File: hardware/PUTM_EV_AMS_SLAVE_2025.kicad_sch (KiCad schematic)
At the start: 19 parts, among them J1 M80-5100405, J2 M80-5100405, J4 IDC24

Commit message: routing 80-90% done
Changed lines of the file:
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@@
-		(length 2.54)
-		(shape round)
-		(at 257.81 -50.8 180)
-		(fields_autoplaced yes)
-		(effects
-			(font
-				(size 1.27 1.27)
-			)
-			(justify right bottom)
-		)
-		(property "Netclass" "DP_50Ohm"
-			(at 258.5085 -48.26 0)
-			(effects
-				(font
-					(size 1.27 1.27)
-					(italic yes)
-				)
-				(justify left)
-			)
-		)
-	)
-	(netclass_flag ""
 		(length 2.54)
 		(shape round)
@@
 		(length 2.54)
 		(shape round)
-		(at 278.13 -53.34 0)
-		(fields_autoplaced yes)
+		(at 226.06 99.06 180)
+		(effects
+			(font
+				(size 1.27 1.27)
+			)
+			(justify right bottom)
+		)
+		(property "Netclass" "DP_50Ohm"
+			(at 226.06 102.87 90)
+			(effects
+				(font
+					(size 1.27 1.27)
+					(italic yes)
+				)
+				(justify right)
+			)
+		)
+	)
+	(netclass_flag ""
+		(length 2.54)
+		(shape round)
+		(at 34.29 101.6 180)
+		(effects
+			(font
+				(size 1.27 1.27)
+			)
+			(justify right bottom)
+		)
+		(property "Netclass" "DP_50Ohm"
+			(at 34.29 105.41 90)
+			(effects
+				(font
+					(size 1.27 1.27)
+					(italic yes)
+				)
+				(justify right)
+			)
+		)
+	)
+	(netclass_flag ""
+		(length 2.54)
+		(shape round)
+		(at 261.62 93.98 0)
 		(effects
 			(font
@@
 		)
 		(property "Netclass" "DP_50Ohm"
-			(at 278.8285 -55.88 0)
-			(effects
-				(font
-					(size 1.27 1.27)
-					(italic yes)
-				)
-				(justify left)
-			)
-		)
-	)
-	(netclass_flag ""
-		(length 2.54)
-		(shape round)
-		(at 226.06 99.06 180)
-		(effects
-			(font
-				(size 1.27 1.27)
-			)
-			(justify right bottom)
-		)
-		(property "Netclass" "DP_50Ohm"
-			(at 226.06 102.87 90)
-			(effects
-				(font
-					(size 1.27 1.27)
-					(italic yes)
-				)
-				(justify right)
-			)
-		)
-	)
-	(netclass_flag ""
-		(length 2.54)
-		(shape round)
-		(at 34.29 101.6 180)
-		(effects
-			(font
-				(size 1.27 1.27)
-			)
-			(justify right bottom)
-		)
-		(property "Netclass" "DP_50Ohm"
-			(at 34.29 105.41 90)
-			(effects
-				(font
-					(size 1.27 1.27)
-					(italic yes)
-				)
-				(justify right)
-			)
-		)
-	)
-	(netclass_flag ""
-		(length 2.54)
-		(shape round)
-		(at 261.62 93.98 0)
-		(effects
-			(font
-				(size 1.27 1.27)
-			)
-			(justify left bottom)
-		)
-		(property "Netclass" "DP_50Ohm"
 			(at 261.62 80.01 90)
 			(effects
@@
 				)
 				(justify right)
-			)
-		)
-	)
-	(netclass_flag ""
-		(length 2.54)
-		(shape round)
-		(at 278.13 -50.8 180)
-		(fields_autoplaced yes)
-		(effects
-			(font
-				(size 1.27 1.27)
-			)
-			(justify right bottom)
-		)
-		(property "Netclass" "DP_50Ohm"
-			(at 278.8285 -48.26 0)
-			(effects
-				(font
-					(size 1.27 1.27)
-					(italic yes)
-				)
-				(justify left)
 			)
 		)
@@
 				)
 				(justify right)
-			)
-		)
-	)
-	(netclass_flag ""
-		(length 2.54)
-		(shape round)
-		(at 257.81 -53.34 0)
-		(fields_autoplaced yes)
-		(effects
-			(font
-				(size 1.27 1.27)
-			)
-			(justify left bottom)
-		)
-		(property "Netclass" "DP_50Ohm"
-			(at 258.5085 -55.88 0)
-			(effects
-				(font
-					(size 1.27 1.27)
-					(italic yes)
-				)
-				(justify left)
 			)
 		)
@@
 		(dnp no)
 		(property "Reference" "R55"
-			(at 189.23 91.2114 90)
+			(at 189.23 88.9 90)
 			(effects
 				(font
@@
 		)
 		(property "Value" "1k"
-			(at 189.23 88.9 90)
-			(effects
-				(font
+			(at 189.23 91.44 90)
+			(effects
+				(font

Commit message: bom update
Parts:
- C46, C47, C48, C49: Mouser Part Number (none) -> 581-06033A221JAT2A
- J4: Mouser Part Number (none) -> 737-BHR-24-VSG-SMT
- L1, L2: Mouser Part Number (none) -> 673-PE-1812AGC101STS
- R55, R58: Mouser Part Number 603-RT0603FRE07330RL -> --
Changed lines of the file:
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@@
+			)
+		)
+		(property "Arrow Part Number" ""
+			(at 144.78 41.91 0)
+			(effects
+				(font
+					(size 1.27 1.27)
+				)
+				(hide yes)
+			)
+		)
+		(property "Arrow Price/Stock" ""
+			(at 144.78 41.91 0)
+			(effects
+				(font
+					(size 1.27 1.27)
+				)
+				(hide yes)
+			)
+		)
+		(property "Mouser Part Number" "737-BHR-24-VSG-SMT"
+			(at 144.78 41.91 0)
+			(effects
+				(font
+					(size 1.27 1.27)
+				)
+				(hide yes)
 			)
 		)
@@
 			)
 		)
-		(property "Mouser Part Number" "603-RT0603FRE07330RL"
+		(property "Mouser Part Number" "--"
 			(at 189.23 93.98 0)
 			(effects
@@
 		)
 		(property "TME Electronic Components Price/Stock" ""
+			(at 25.4 91.44 0)
+			(effects
+				(font
+					(size 1.27 1.27)
+				)
+				(hide yes)
+			)
+		)
+		(property "Arrow Part Number" ""
+			(at 25.4 91.44 0)
+			(effects
+				(font
+					(size 1.27 1.27)
+				)
+				(hide yes)
+			)
+		)
+		(property "Arrow Price/Stock" ""
 			(at 25.4 91.44 0)
 			(effects
@@
 			)
 		)
+		(property "Arrow Part Number" ""
+			(at 238.76 97.79 0)
+			(effects
+				(font
+					(size 1.27 1.27)
+				)
+				(hide yes)
+			)
+		)
+		(property "Arrow Price/Stock" ""
+			(at 238.76 97.79 0)
+			(effects
+				(font
+					(size 1.27 1.27)
+				)
+				(hide yes)
+			)
+		)
+		(property "Mouser Part Number" "673-PE-1812AGC101STS"
+			(at 238.76 97.79 0)
+			(effects
+				(font
+					(size 1.27 1.27)
+				)
+				(hide yes)
+			)
+		)
 		(pin "1"
 		)
@@
 			)
 		)
+		(property "Arrow Part Number" ""
+			(at 196.85 104.14 0)
+			(effects
+				(font
+					(size 1.27 1.27)
+				)
+				(hide yes)
+			)
+		)
+		(property "Arrow Price/Stock" ""
+			(at 196.85 104.14 0)
+			(effects
+				(font
+					(size 1.27 1.27)
+				)
+				(hide yes)
+			)
+		)
+		(property "Mouser Part Number" "581-06033A221JAT2A"
+			(at 196.85 104.14 0)
+			(effects
+				(font
+					(size 1.27 1.27)
+				)
+				(hide yes)
+			)
+		)
 		(pin "2"
 		)
@@
 			)
 		)
+		(property "Arrow Part Number" ""
+			(at 57.15 97.79 0)
+			(effects
+				(font
+					(size 1.27 1.27)
+				)
+				(hide yes)
+			)
+		)
+		(property "Arrow Price/Stock" ""
+			(at 57.15 97.79 0)
+			(effects
+				(font
+					(size 1.27 1.27)
+				)
+				(hide yes)
+			)
+		)
+		(property "Mouser Part Number" "673-PE-1812AGC101STS"
+			(at 57.15 97.79 0)
+			(effects
+				(font
+					(size 1.27 1.27)
+				)
+				(hide yes)
+			)
+		)
 		(pin "1"
 		)
@@
 		)
 		(property "TME Electronic Components Price/Stock" ""
+			(at 86.36 104.14 0)
+			(effects
+				(font
+					(size 1.27 1.27)
+				)
+				(hide yes)
+			)
+		)
+		(property "Arrow Part Number" ""
+			(at 86.36 104.14 0)
+			(effects
+				(font
+					(size 1.27 1.27)
+				)
+				(hide yes)
+			)
+		)
+		(property "Arrow Price/Stock" ""
+			(at 86.36 104.14 0)
+			(effects
+				(font
+					(size 1.27 1.27)
+				)
+				(hide yes)
+			)
+		)
+		(property "Mouser Part Number" "581-06033A221JAT2A"
 			(at 86.36 104.14 0)
 			(effects
@@
 			)
 		)
+		(property "Arrow Part Number" ""
+			(at 270.51 91.44 0)
+			(effects
+				(font
+					(size 1.27 1.27)
+				)
+				(hide yes)
+			)
+		)
+		(property "Arrow Price/Stock" ""
+			(at 270.51 91.44 0)
+			(effects
+				(font
+					(size 1.27 1.27)
+				)
+				(hide yes)
+			)
+		)
 		(pin "3"
 		)
@@
 			)
 		)
-		(property "Mouser Part Number" "603-RT0603FRE07330RL"
+		(property "Mouser Part Number" "--"
 			(at 105.41 93.98 0)
 			(effects
@@
 		)
 		(property "TME Electronic Components Price/Stock" ""
+			(at 97.79 104.14 0)
+			(effects
+				(font
+					(size 1.27 1.27)
+				)
+				(hide yes)
+			)
+		)
+		(property "Arrow Part Number" ""
+			(at 97.79 104.14 0)
+			(effects
+				(font
+					(size 1.27 1.27)
+				)
+				(hide yes)
+			)
+		)
+		(property "Arrow Price/Stock" ""
+			(at 97.79 104.14 0)
+			(effects
+				(font
+					(size 1.27 1.27)
+				)
+				(hide yes)
+			)
+		)
+		(property "Mouser Part Number" "581-06033A221JAT2A"
 			(at 97.79 104.14 0)
 			(effects
@@
 			(at 208.28 104.14 0)
 			(effects
+				(font
+					(size 1.27 1.27)
+				)
+				(hide yes)
+			)
+		)
+		(property "Arrow Part Number" ""
+			(at 208.28 104.14 0)
+			(effects
+				(font
+					(size 1.27 1.27)
+				)
+				(hide yes)
+			)
+		)
+		(property "Arrow Price/Stock" ""
+			(at 208.28 104.14 0)
+			(effects
+				(font
+					(size 1.27 1.27)
+				)
+				(hide yes)
+			)
+		)
+		(property "Mouser Part Number" "581-06033A221JAT2A"
+			(at 208.28 104.14 0)
+			(effects

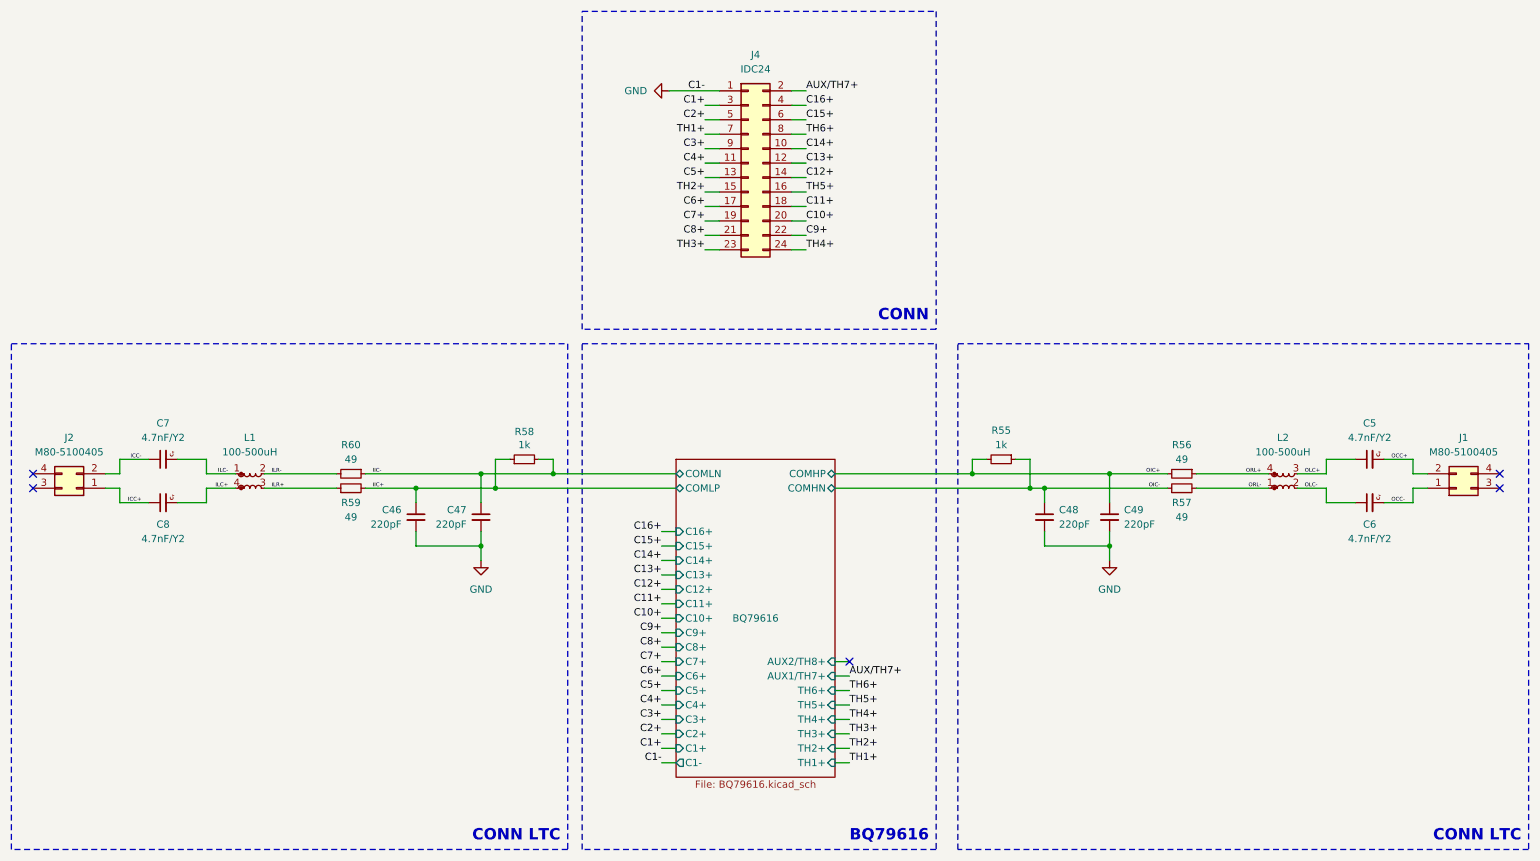
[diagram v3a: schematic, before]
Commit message: removed cmc, added tvs on com channels
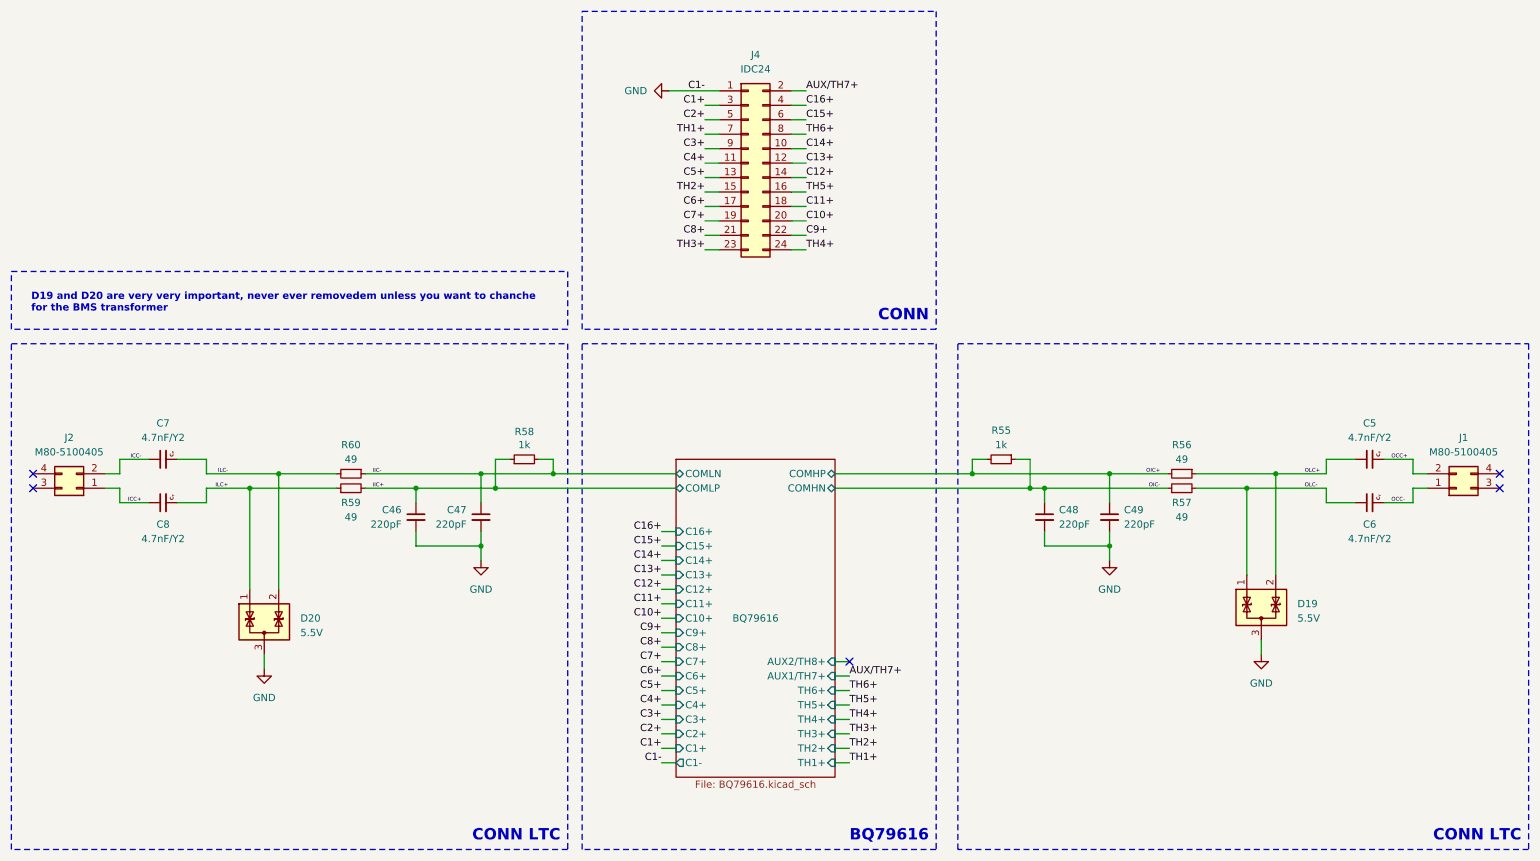
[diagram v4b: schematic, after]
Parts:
- removed L1, L2: 100-500uH, Inductor_SMD:L_CommonModeChoke_Coilcraft_1812CAN, symbol Device:L_Coupled_Small_1243
- added D19, D20: 5.5V, Package_TO_SOT_SMD:SOT-23-3, symbol Power_Protection:ESDA5V3L
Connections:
- net ILR+ is gone; now on net ILC+: R59.1
- net ILR- is gone; now on net ILC-: R60.2
- net ORL+ is gone; now on net OLC+: R56.1
- net ORL- is gone; now on net OLC-: R57.2
- net GND: now also D19.3 (A), D20.3 (A)
- net ILC+: now also D20.1 (K)
- net ILC-: now also D20.2 (K)
- net OLC+: now also D19.2 (K)
- net OLC-: now also D19.1 (K)
